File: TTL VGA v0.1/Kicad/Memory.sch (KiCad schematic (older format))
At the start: 17 parts

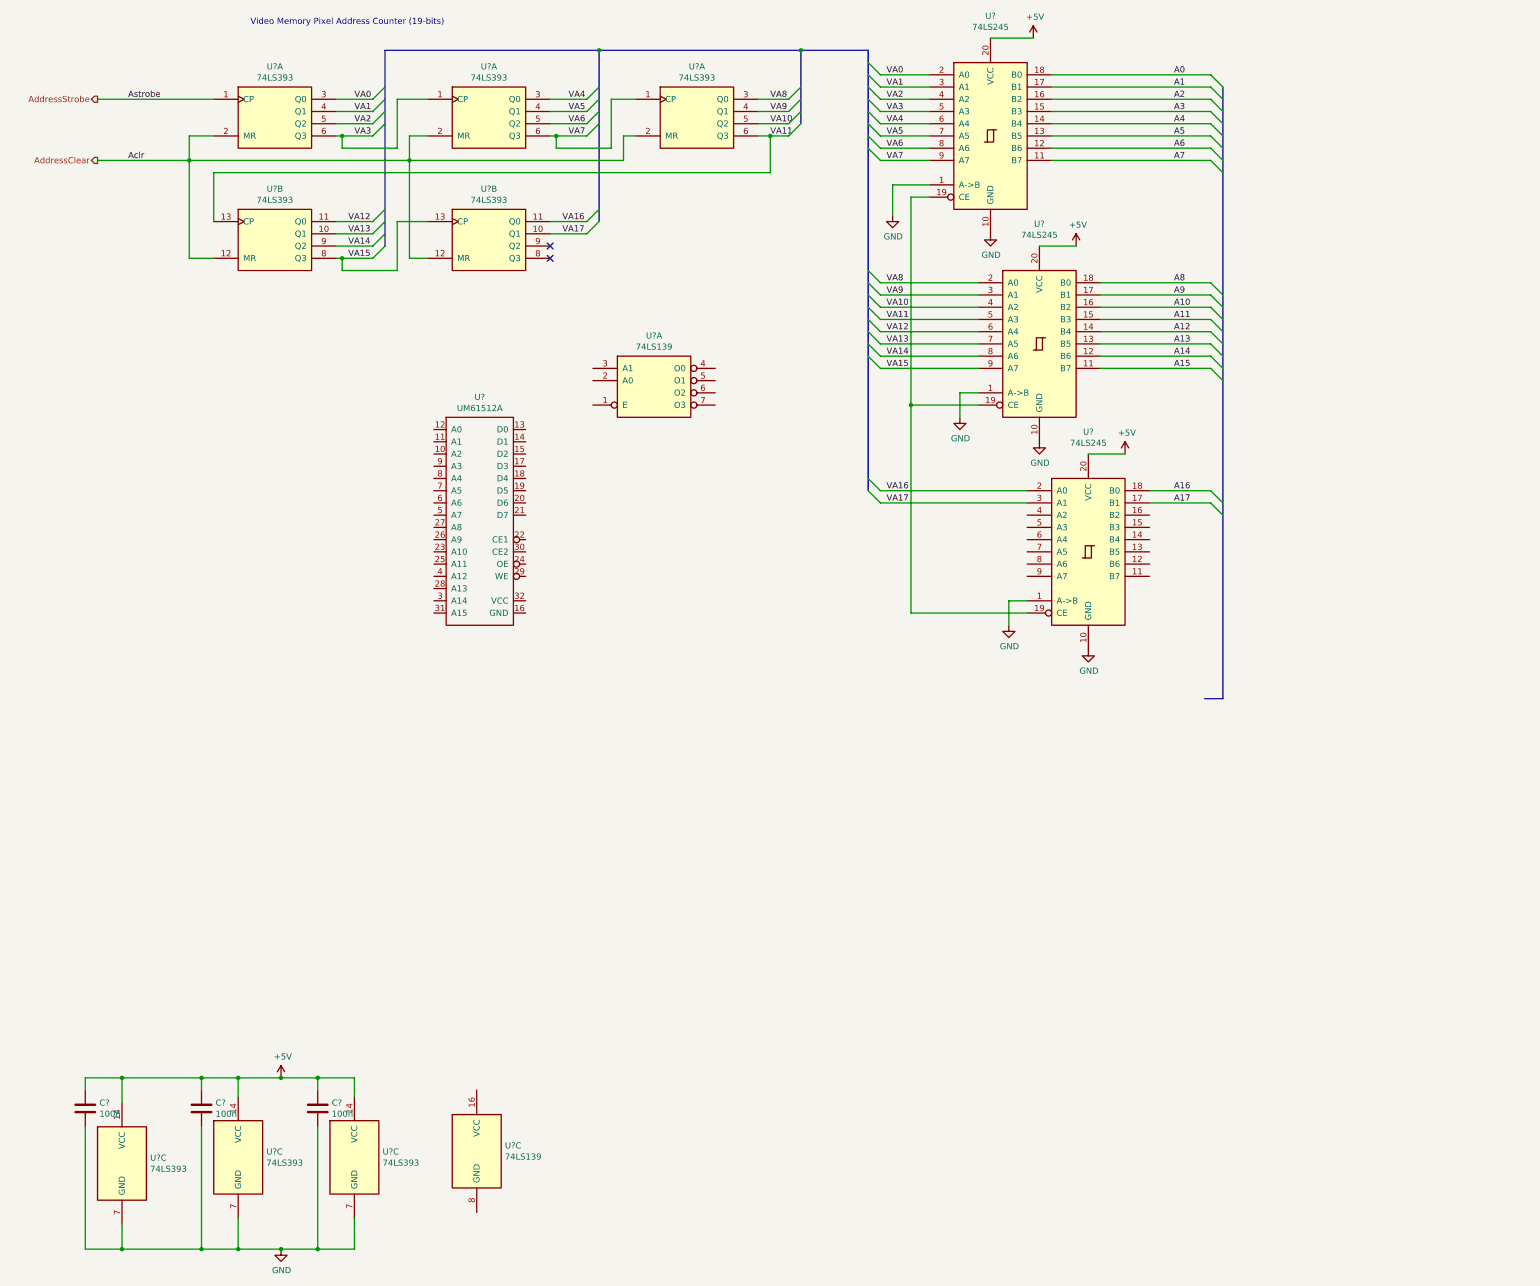
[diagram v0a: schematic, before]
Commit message: binary counter cupl
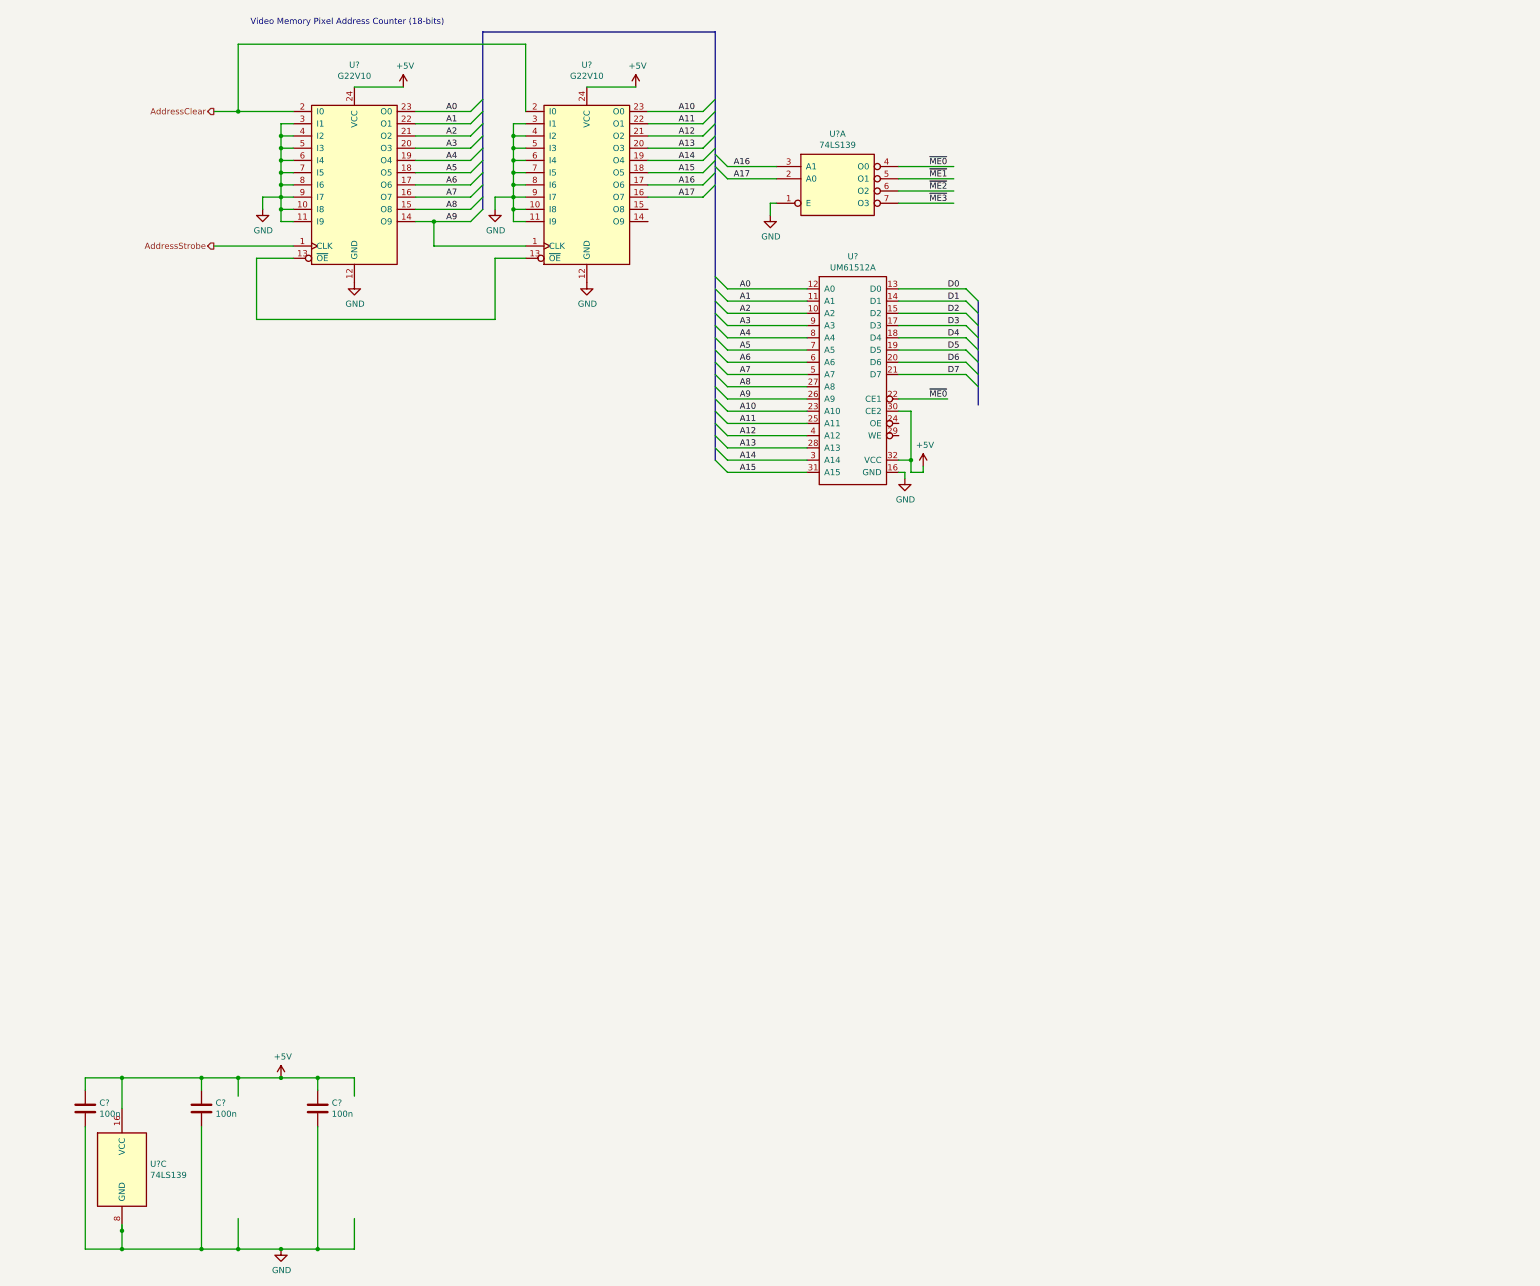
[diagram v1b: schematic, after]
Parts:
- removed U? (x8): 74LS393, symbol 74xx:74LS393
- removed U? (x3): 74LS245, symbol 74xx:74LS245
- added U? (x2): G22V10, symbol Logic_Programmable:PAL20RS10
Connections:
- net labels added: D0, D1, D2, D3, D4, D5, D6, D7, ~ME0, ~ME1, ~ME2, ~ME3
- net labels removed: Aclr, Astrobe, VA0, VA1, VA10, VA11, VA12, VA13, VA14, VA15, VA16, VA17, VA2, VA3, VA4, VA5, VA6, VA7, VA8, VA9
- wire segments 125 -> 138
- no-connect marks 2 -> 0
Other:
- note added: "Video Memory Pixel Address Counter (18-bits)"
- note removed: "Video Memory Pixel Address Counter (19-bits)"
- moved on the sheet: U?, U?A, U?C

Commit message: tweaks
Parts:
- removed U? (x2): G22V10, symbol Logic_Programmable:PAL20RS10
- added C12, C13: 100n, symbol Device:C
- added U10: UM61512A, symbol UM61512A:UM61512A
- added U11, U13, U14: 74LS245, symbol 74xx:74LS245
- added U12: 74LS374, symbol 74xx:74LS374
- added U6, U7: G22V10, symbol 22V10:G22V10
- gave numbers to parts that had none: 5
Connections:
- net labels added: BD0, BD1, BD2, BD3, BD4, BD5, BD6, BD7, BusAddress, BusControl, BusData, MA0, MA1, MA10, MA11, MA2, MA3, MA4, MA5, MA6, MA7, MA8, MA9, PixelData, ~AddressEnable
- wire segments 138 -> 288
- no-connect marks 0 -> 8
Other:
- note added: "Z80 interfaces through a 4k Memory Page. \nThe location (bit address) of this memory page is determined by the Bus Decoder.\n\nThe Control Register provides the upper 6 bits A12..A17 of the\nVRAM address and can only be changed through an IO write.\nThe IO address (A0-A7) is also determined by the Bus Decoder."
- moved on the sheet: U8A, U9
